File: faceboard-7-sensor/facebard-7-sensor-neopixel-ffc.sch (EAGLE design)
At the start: 32 parts, among them Q1 QRE1113, Q2 QRE1113, Q3 QRE1113, Q4 QRE1113, Q5 QRE1113, Q6 QRE1113, Q7 QRE1113, U1 CD4051BE

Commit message: tidy
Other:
- note added: "Solder Junction"
- note removed: "Soulder Junction"
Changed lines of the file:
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@@
 <sheet>
 <plain>
-<text x="41.656" y="109.22" size="1.778" layer="91">Soulder
+<text x="41.656" y="109.22" size="1.778" layer="91">Solder
 Junction</text>
 </plain>
@@
 </instance>
 <instance part="U1" gate="A" x="68.58" y="109.22" smashed="yes">
-<attribute name="VALUE" x="60.4774" y="82.7786" size="2.0828" layer="96" ratio="6" rot="SMR0"/>
+<attribute name="VALUE" x="90.9574" y="82.7786" size="2.0828" layer="96" ratio="6" rot="SMR0"/>
 </instance>
 <instance part="SUPPLY10" gate="G$1" x="71.12" y="139.7" smashed="yes">

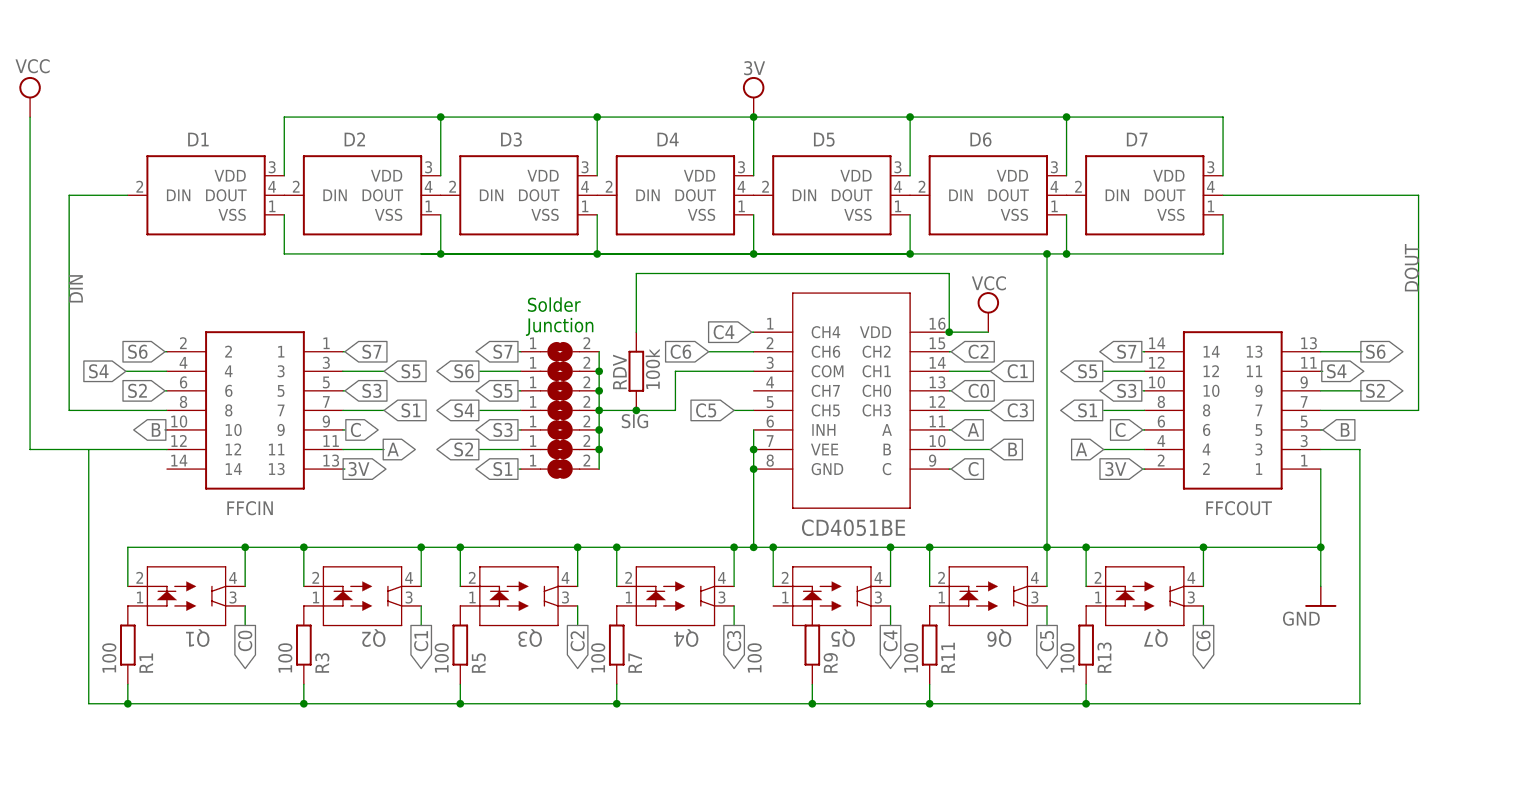
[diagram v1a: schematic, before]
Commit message: rewire mini leds and dividing resistors
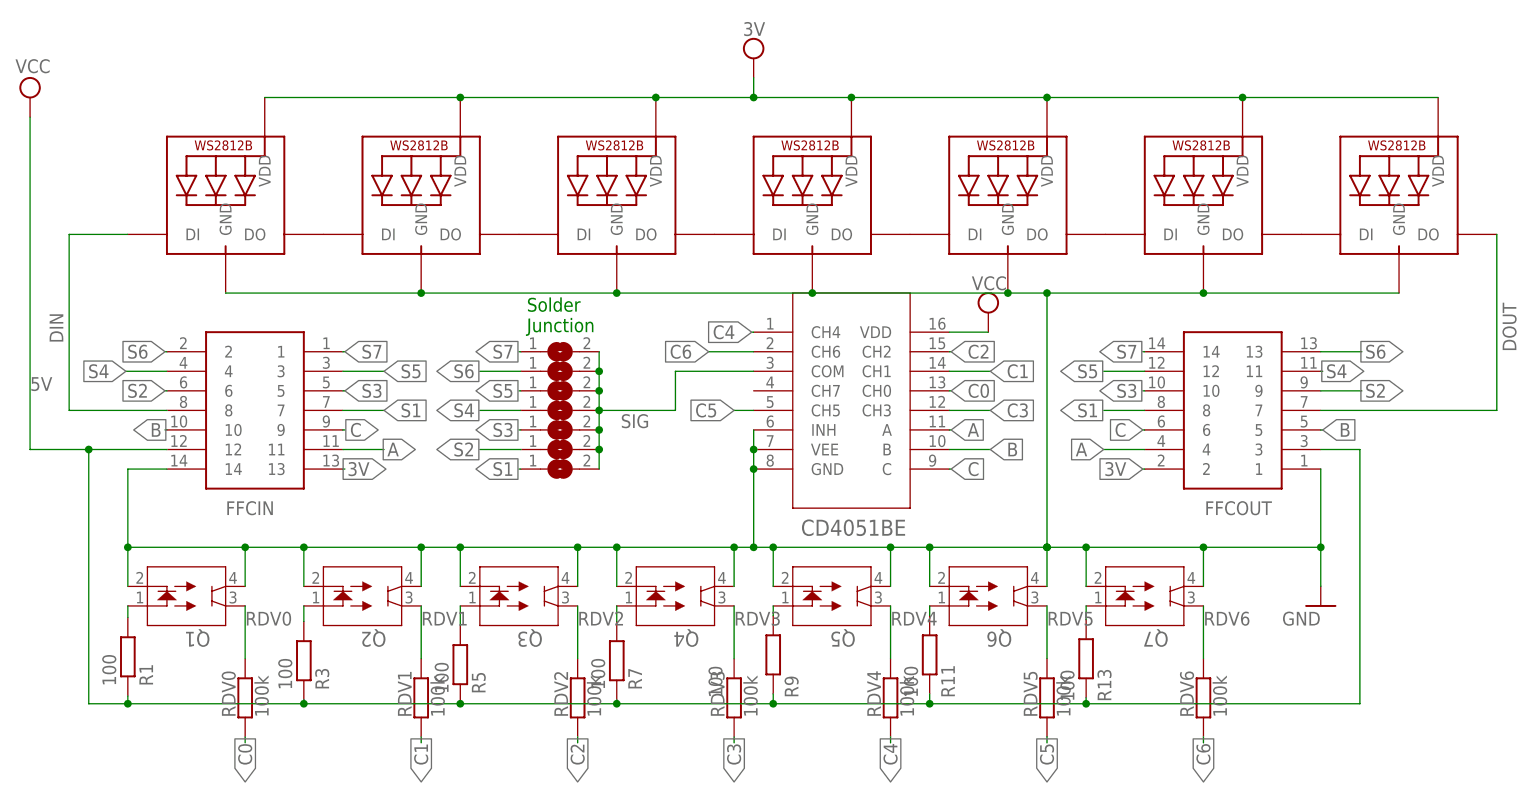
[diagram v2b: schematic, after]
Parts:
- removed D1, D2, D3, D4, D5, D6, D7: 1655, 1655:1655
- removed RDV: 100k, rcl:R-EU_0207/10
- added LED1, LED2, LED3, LED4, LED5, LED6, LED7: WS2812B3535, adafruit:WS2812B3535
- added RDV0, RDV1, RDV2, RDV3, RDV4, RDV5, RDV6: 100k, rcl:R-EU_0207/10
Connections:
- removed net N$15: D6.DOUT, D7.DIN
- removed net N$16: D1.DOUT, D2.DIN
- removed net N$17: D2.DOUT, D3.DIN
- removed net N$18: D3.DOUT, D4.DIN
- removed net N$19: D4.DOUT, D5.DIN
- removed net N$2: FFCOUT.3, R1.1, R11.1, R13.1, R3.1, R5.1, R7.1, R9.1
- removed net N$20: D5.DOUT, D6.DIN
- removed net VCC: FFCIN.12, RDV.2, U1.VDD
- new net 5V: FFCIN.12, FFCOUT.3, R1.1, R11.1, R13.1, R3.1, R5.1, R7.1, R9.1, U1.VDD
- new net N$10: LED5.DO, LED6.DI
- new net N$12: LED6.DO, LED7.DI
- new net N$14: Q5.1, R9.2
- new net N$4: LED1.DO, LED2.DI
- new net N$6: LED2.DO, LED3.DI
- new net N$8: LED3.DO, LED4.DI
- new net N$9: LED4.DO, LED5.DI
- new net RDV0: Q1.3, RDV0.2
- new net RDV1: Q2.3, RDV1.2
- new net RDV2: Q3.3, RDV2.2
- new net RDV3: Q4.3, RDV3.2
- new net RDV4: Q5.3, RDV4.2
- new net RDV5: Q6.3, RDV5.2
- new net RDV6: Q7.3, RDV6.2
- net 3V: now also LED1.VDD, LED2.VDD, LED3.VDD, LED4.VDD, LED5.VDD, LED6.VDD, LED7.VDD; no longer D1.VDD, D2.VDD, D3.VDD, D4.VDD, D5.VDD, D6.VDD, D7.VDD
- net C0: now also RDV0.1; no longer Q1.3
- net C1: now also RDV1.1; no longer Q2.3
- net C2: now also RDV2.1; no longer Q3.3
- net C3: now also RDV3.1; no longer Q4.3
- net C4: now also RDV4.1; no longer Q5.3
- net C5: now also RDV5.1; no longer Q6.3
- net C6: now also RDV6.1; no longer Q7.3
- net DIN: now also LED1.DI; no longer D1.DIN
- net DOUT: now also LED7.DO; no longer D7.DOUT
- net GND: now also FFCIN.14, LED1.GND, LED2.GND, LED3.GND, LED4.GND, LED5.GND, LED6.GND, LED7.GND; no longer D1.VSS, D2.VSS, D3.VSS, D4.VSS, D5.VSS, D6.VSS, D7.VSS
- net SIG: no longer RDV.1
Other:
- moved on the sheet: R1, R11, R13, R3, R5, R7, R9

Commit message: fix signal routing
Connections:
- removed net RDV0: Q1.3, RDV0.2
- removed net RDV1: Q2.3, RDV1.2
- removed net RDV2: Q3.3, RDV2.2
- removed net RDV3: Q4.3, RDV3.2
- removed net RDV4: Q5.3, RDV4.2
- removed net RDV5: Q6.3, RDV5.2
- removed net RDV6: Q7.3, RDV6.2
- net 5V: now also RDV0.1, RDV1.1, RDV2.1, RDV3.1, RDV4.1, RDV5.1, RDV6.1
- net C0: now also Q1.3, RDV0.2; no longer RDV0.1
- net C1: now also Q2.3, RDV1.2; no longer RDV1.1
- net C2: now also Q3.3, RDV2.2; no longer RDV2.1
- net C3: now also Q4.3, RDV3.2; no longer RDV3.1
- net C4: now also Q5.3, RDV4.2; no longer RDV4.1
- net C5: now also Q6.3, RDV5.2; no longer RDV5.1
- net C6: now also Q7.3, RDV6.2; no longer RDV6.1
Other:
- moved on the sheet: RDV0, RDV1, RDV2, RDV3, RDV4, RDV5, RDV6
